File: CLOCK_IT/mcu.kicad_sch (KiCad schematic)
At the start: 25 parts, among them IC1 APS6404L-3SQR-SN, U1 ESP32-S3R8, U2 W25Q128JVSIQ

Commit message: :white_check_mark: Halffway here
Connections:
- net GND: now also U1.57 (GND)
- net USB_D+ renamed USB_DP
- net USB_D- renamed USB_DN
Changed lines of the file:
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@@
+	(wire
+		(pts
+			(xy 152.4 130.81) (xy 154.94 130.81)
+		)
+		(stroke
+			(width 0)
+			(type default)
+		)
+	)
 	(wire
 		(pts
@@
 		)
 	)
+	(label "USB_DP"
+		(at 162.56 102.87 180)
+		(effects
+			(font
+				(size 1.27 1.27)
+			)
+			(justify right bottom)
+		)
+	)
 	(label "Flash D"
 		(at 92.71 125.73 0)
@@
 		)
 	)
-	(label "USB_D+"
-		(at 162.56 102.87 180)
-		(effects
-			(font
-				(size 1.27 1.27)
-			)
-			(justify right bottom)
-		)
-	)
 	(label "XTAL_N"
 		(at 21.59 29.21 0)
@@
 			)
 			(justify left bottom)
+		)
+	)
+	(hierarchical_label "USB_DN"
+		(shape input)
+		(at 162.56 100.33 0)
+		(effects
+			(font
+				(size 1.27 1.27)
+			)
+			(justify left)
+		)
+	)
+	(hierarchical_label "USB_DP"
+		(shape input)
+		(at 162.56 102.87 0)
+		(effects
+			(font
+				(size 1.27 1.27)
+			)
+			(justify left)
 		)
 	)
@@
 					(unit 1)
 				)
+			)
+		)
+	)
+	(symbol
+		(lib_id "power:GND")
+		(at 154.94 130.81 0)
+		(unit 1)
+		(exclude_from_sim no)
+		(in_bom yes)
+		(on_board yes)
+		(dnp no)
+		(fields_autoplaced yes)
+		(property "Reference" "#PWR078"
+			(at 154.94 137.16 0)
+			(effects
+				(font
+					(size 1.27 1.27)
+				)
+				(hide yes)
+			)
+		)
+		(property "Value" "GND"
+			(at 154.94 135.89 0)
+			(effects
+				(font
+					(size 1.27 1.27)
+				)
+			)
+		)
+		(property "Footprint" ""
+			(at 154.94 130.81 0)
+			(effects
+				(font
+					(size 1.27 1.27)
+				)
+				(hide yes)
+			)
+		)
+		(property "Datasheet" ""
+			(at 154.94 130.81 0)
+			(effects
+				(font
+					(size 1.27 1.27)
+				)
+				(hide yes)
+			)
+		)
+		(property "Description" "Power symbol creates a global label with name \"GND\" , ground"
+			(at 154.94 130.81 0)
+			(effects
+				(font
+					(size 1.27 1.27)
+				)
+				(hide yes)
+			)
+		)
+		(pin "1"
+		)
+		(instances
+			(project "CLOCK_IT"
+				(path "/6c8f4e2a-0be1-4eb1-92e1-07339040f4c9/25a0942f-4692-4437-8e26-71d966c353a5"
+					(reference "#PWR078")
+					(unit 1)
+				)

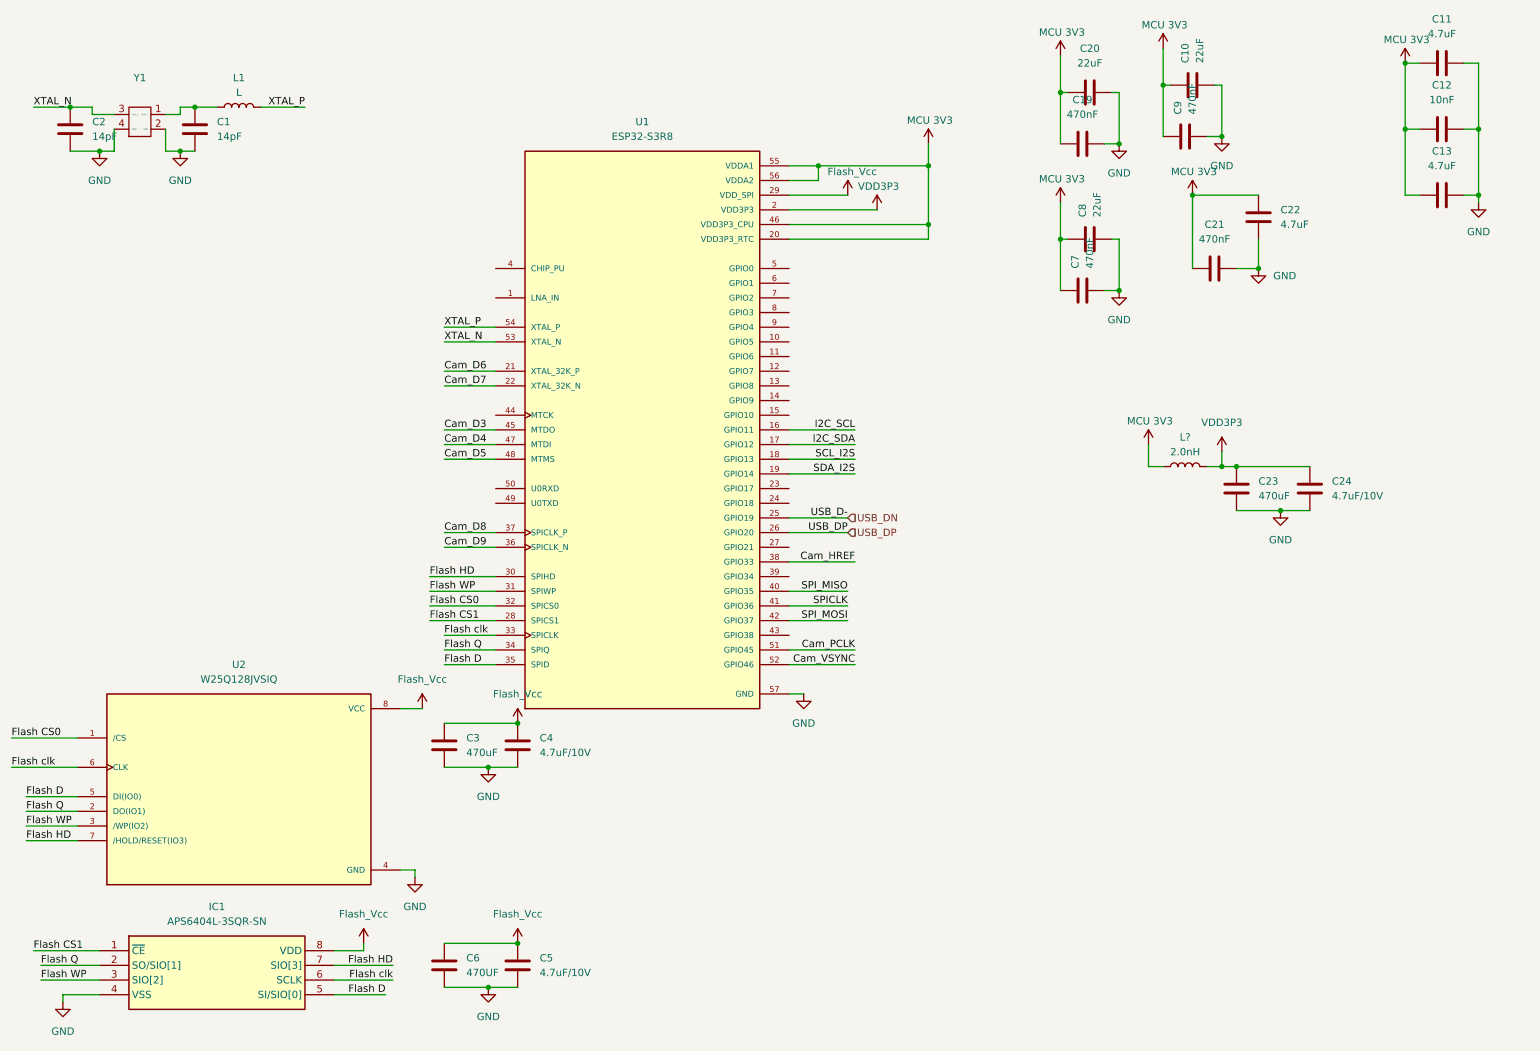
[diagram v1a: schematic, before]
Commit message: :white_check_mark: CHANGES in 12C pull up resisors
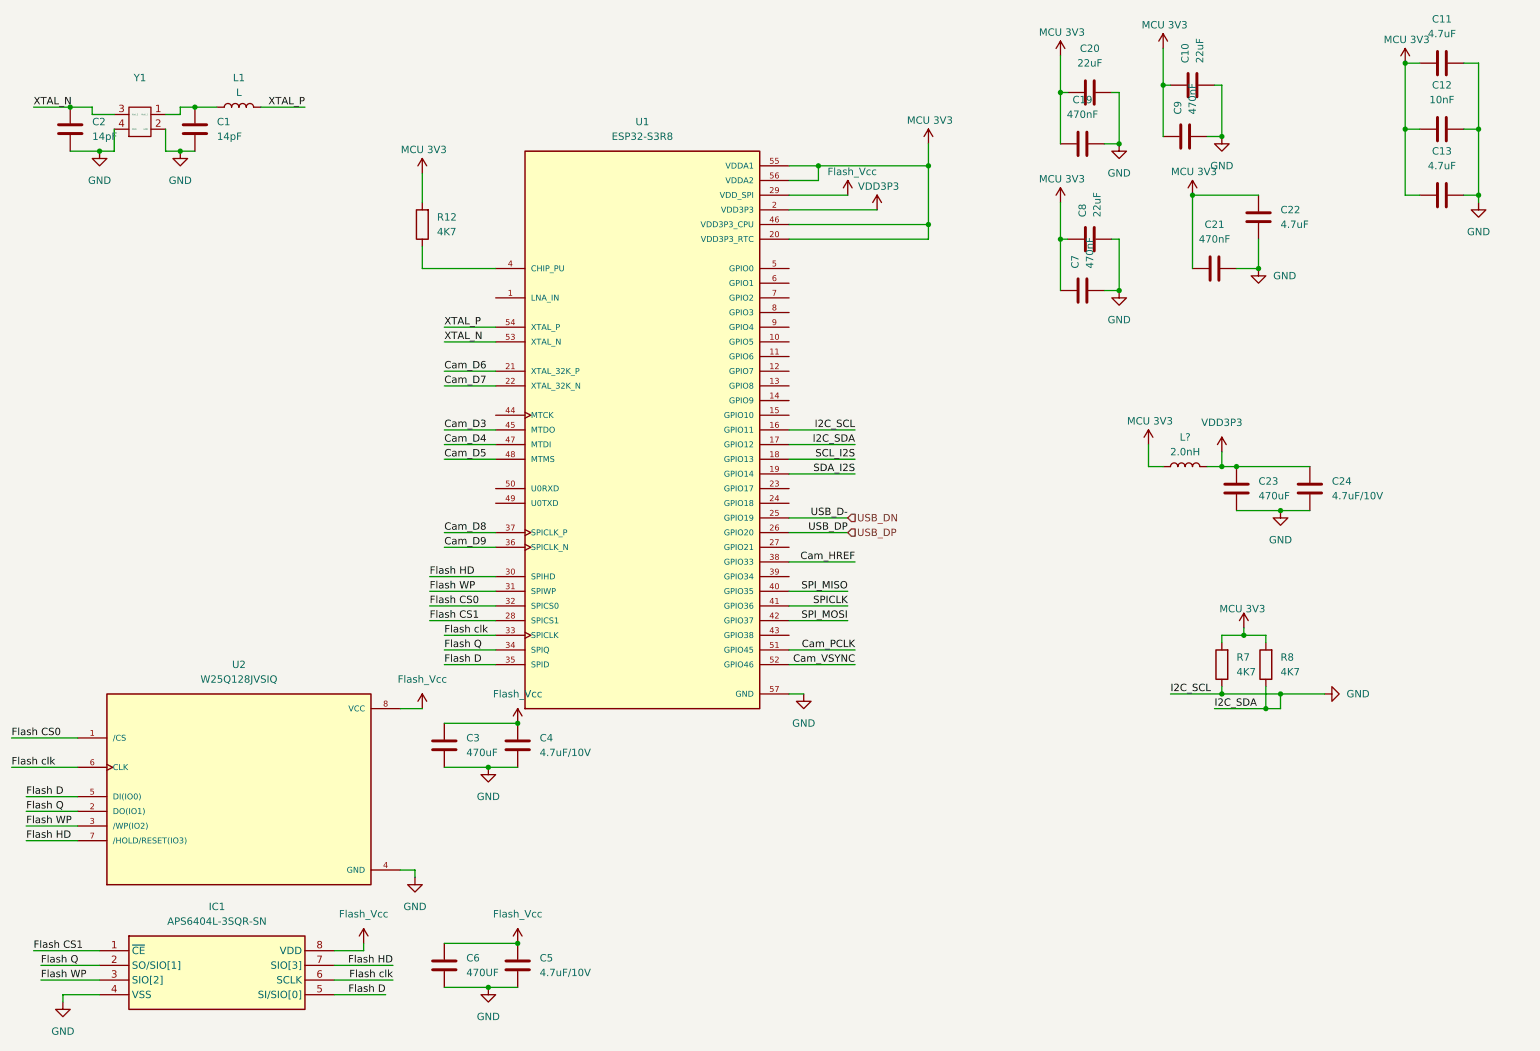
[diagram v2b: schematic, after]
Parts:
- added R12, R7, R8: 4K7, symbol Device:R
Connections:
- net I2C_SCL is gone; now on net GND: U1.16 (GPIO11)
- net I2C_SDA is gone; now on net GND: U1.17 (GPIO12)
- net GND: now also R7.1, R8.1
- net MCU 3V3: now also R12.2, R7.2, R8.2
- net at U1.4 (CHIP_PU): now also R12.1

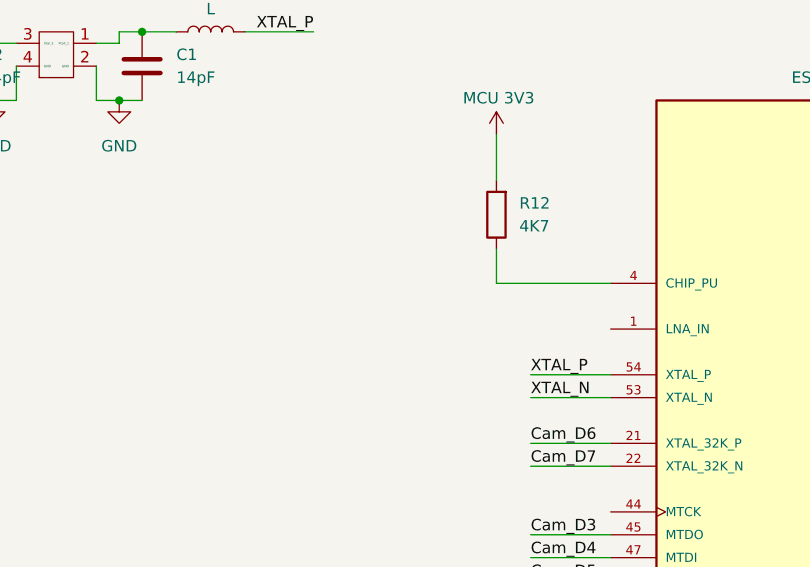
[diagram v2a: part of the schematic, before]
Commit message: :white_check_mark: added tacktile chip pu switch
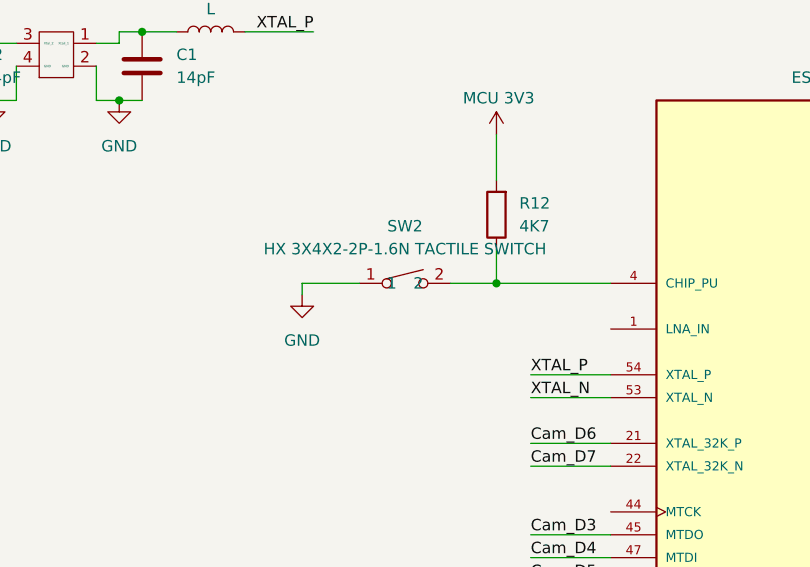
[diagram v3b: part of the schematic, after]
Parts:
- added SW2: HX 3X4X2-2P-1.6N TACTILE SWITCH, easyeda2kicad:KEY-SMD_L4.0-W3.0-LS4.9-1, symbol HX 3x4x2-2P-1.6N TACTILE SWITCH:HX3X4X2-2P-1.6NTACTILESWITCH
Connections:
- net GND: now also SW2.1
- net at R12.1, U1.4 (CHIP_PU): now also SW2.2
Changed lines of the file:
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@@
 	)
 	(junction
+		(at 88.9 57.15)
+		(diameter 0)
+		(color 0 0 0 0)
+	)
+	(junction
 		(at 229.87 91.44)
 		(diameter 0)
@@
 	(wire
 		(pts
+			(xy 67.31 57.15) (xy 73.66 57.15)
+		)
+		(stroke
+			(width 0)
+			(type default)
+		)
+	)
+	(wire
+		(pts
 			(xy 90.17 110.49) (xy 101.6 110.49)
 		)
@@
 	(wire
 		(pts
+			(xy 83.82 57.15) (xy 88.9 57.15)
+		)
+		(stroke
+			(width 0)
+			(type default)
+		)
+	)
+	(wire
+		(pts
 			(xy 209.55 52.07) (xy 208.28 52.07)
 		)
@@
 	(wire
 		(pts
+			(xy 67.31 58.42) (xy 67.31 57.15)
+		)
+		(stroke
+			(width 0)
+			(type default)
+		)
+	)
+	(wire
+		(pts
 			(xy 92.71 143.51) (xy 100.33 143.51)
 		)
@@
 	)
 	(symbol
+		(lib_id "HX 3x4x2-2P-1.6N TACTILE SWITCH:HX3X4X2-2P-1.6NTACTILESWITCH")
+		(at 78.74 55.88 0)
+		(unit 1)
+		(exclude_from_sim no)
+		(in_bom yes)
+		(on_board yes)
+		(dnp no)
+		(fields_autoplaced yes)
+		(property "Reference" "SW2"
+			(at 78.74 50.8 0)
+			(effects
+				(font
+					(size 1.27 1.27)
+				)
+			)
+		)
+		(property "Value" "HX 3X4X2-2P-1.6N TACTILE SWITCH"
+			(at 78.74 53.34 0)
+			(effects
+				(font
+					(size 1.27 1.27)
+				)
+			)
+		)
+		(property "Footprint" "easyeda2kicad:KEY-SMD_L4.0-W3.0-LS4.9-1"
+			(at 78.74 64.77 0)
+			(effects
+				(font
+					(size 1.27 1.27)
+				)
+				(hide yes)
+			)
+		)
+		(property "Datasheet" "https://www.lcsc.com/datasheet/C49234124.pdf"
+			(at 78.74 67.31 0)
+			(effects
+				(font
+					(size 1.27 1.27)
+				)
+				(hide yes)
+			)
+		)
+		(property "Description" ""
+			(at 78.74 55.88 0)
+			(effects
+				(font
+					(size 1.27 1.27)
+				)
+				(hide yes)
+			)
+		)
+		(property "Manufacturer" "hanxia(韩下)"
+			(at 78.74 69.85 0)
+			(effects
+				(font
+					(size 1.27 1.27)
+				)
+				(hide yes)
+			)
+		)
+		(property "MPN" "HX 3x4x2-2P-1.6N TACTILE SWITCH"
+			(at 78.74 72.39 0)
+			(effects
+				(font
+					(size 1.27 1.27)
+				)
+				(hide yes)
+			)
+		)
+		(property "LCSC Part" "C49234124"
+			(at 78.74 74.93 0)
+			(effects
+				(font
+					(size 1.27 1.27)
+				)
+				(hide yes)
+			)
+		)
+		(pin "1"
+		)
+		(pin "2"
+		)
+		(instances
+			(project ""
+				(path "/6c8f4e2a-0be1-4eb1-92e1-07339040f4c9/25a0942f-4692-4437-8e26-71d966c353a5"
+					(reference "SW2")
+					(unit 1)
+				)
+			)
+		)
+	)
+	(symbol
 		(lib_id "power:GND")
 		(at 46.99 36.83 0)
@@
 					(unit 1)
 				)
+			)
+		)
+	)
+	(symbol
+		(lib_id "power:GND")
+		(at 67.31 58.42 0)
+		(unit 1)
+		(exclude_from_sim no)
+		(in_bom yes)
+		(on_board yes)
+		(dnp no)
+		(fields_autoplaced yes)
+		(property "Reference" "#PWR082"
+			(at 67.31 64.77 0)
+			(effects
+				(font
+					(size 1.27 1.27)
+				)
+				(hide yes)
+			)
+		)
+		(property "Value" "GND"
+			(at 67.31 63.5 0)
+			(effects
+				(font
+					(size 1.27 1.27)
+				)
+			)
+		)
+		(property "Footprint" ""
+			(at 67.31 58.42 0)
+			(effects
+				(font
+					(size 1.27 1.27)
+				)
+				(hide yes)
+			)
+		)
+		(property "Datasheet" ""
+			(at 67.31 58.42 0)
+			(effects
+				(font
+					(size 1.27 1.27)
+				)
+				(hide yes)
+			)
+		)
+		(property "Description" "Power symbol creates a global label with name \"GND\" , ground"
+			(at 67.31 58.42 0)
+			(effects
+				(font
+					(size 1.27 1.27)
+				)
+				(hide yes)
+			)
+		)
+		(pin "1"
+		)
+		(instances
+			(project "CLOCK_IT"
+				(path "/6c8f4e2a-0be1-4eb1-92e1-07339040f4c9/25a0942f-4692-4437-8e26-71d966c353a5"
+					(reference "#PWR082")
+					(unit 1)
+				)

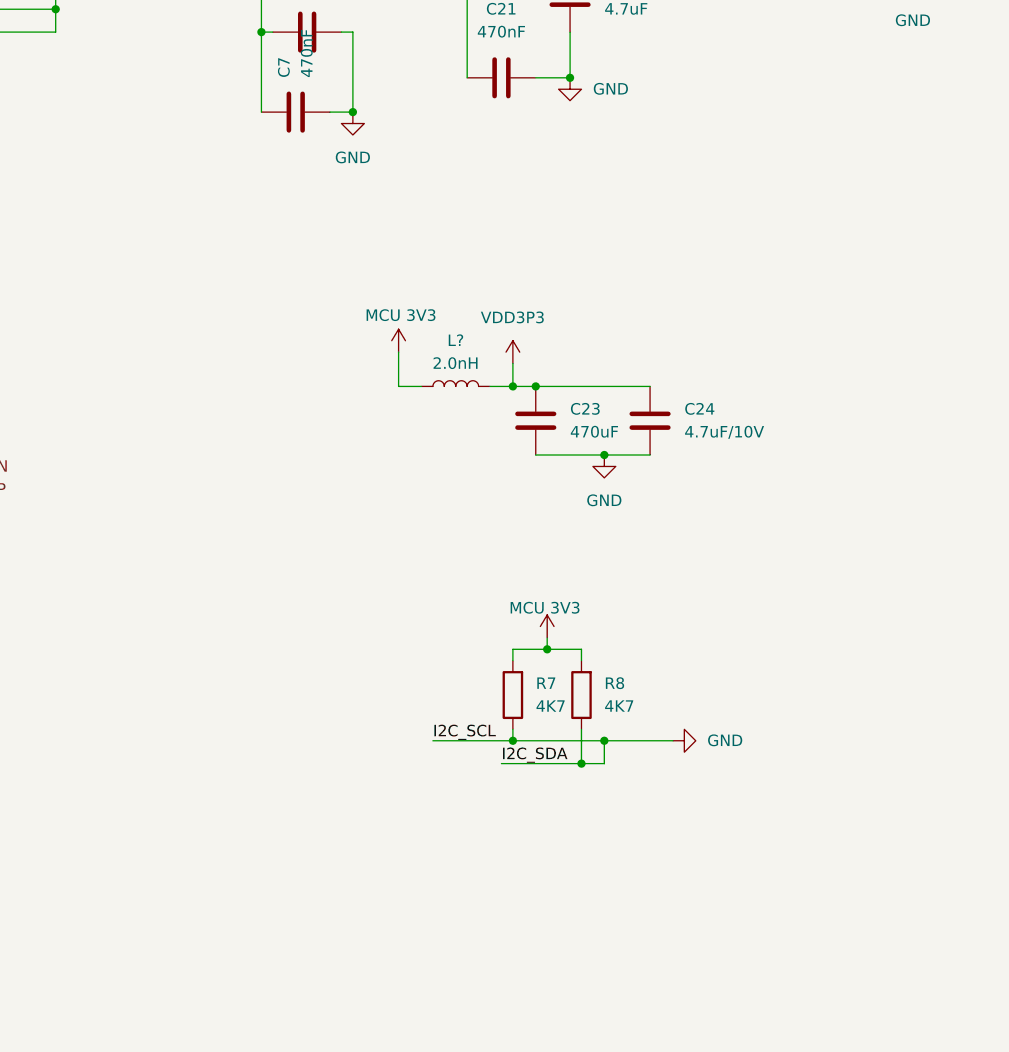
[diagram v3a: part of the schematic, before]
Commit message: :white_check_mark: Correcting I2C address conflicts with an i2c bus switch
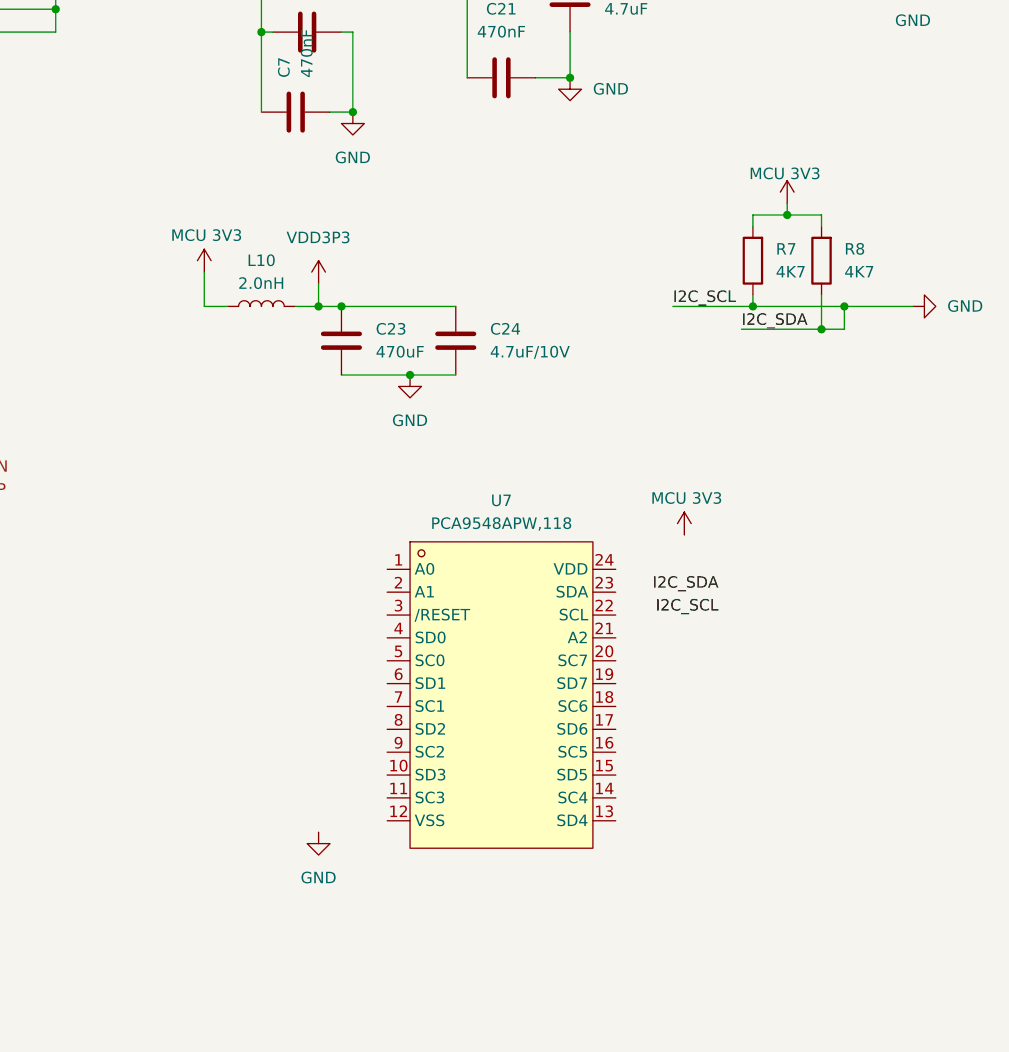
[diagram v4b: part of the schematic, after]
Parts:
- added U7: PCA9548APW,118, easyeda2kicad:TSSOP-24_L7.8-W4.4-P0.65-LS6.4-BL, symbol PCA9548APW,118:PCA9548APW,118
- gave numbers to parts that had none: 1
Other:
- moved on the sheet: C23, C24, L10, R7, R8

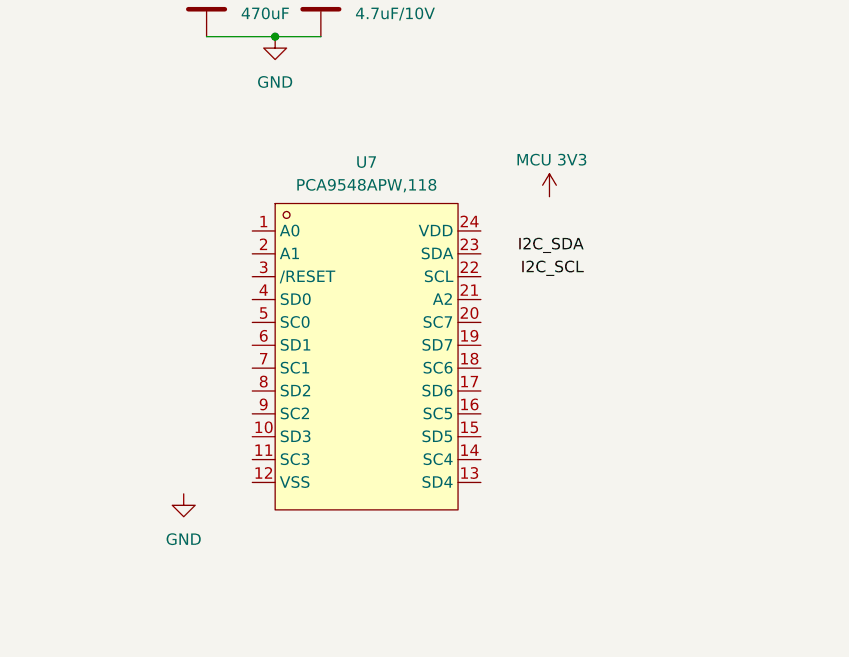
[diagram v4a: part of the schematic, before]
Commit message: :white_check_mark: Connected i2c bus switch
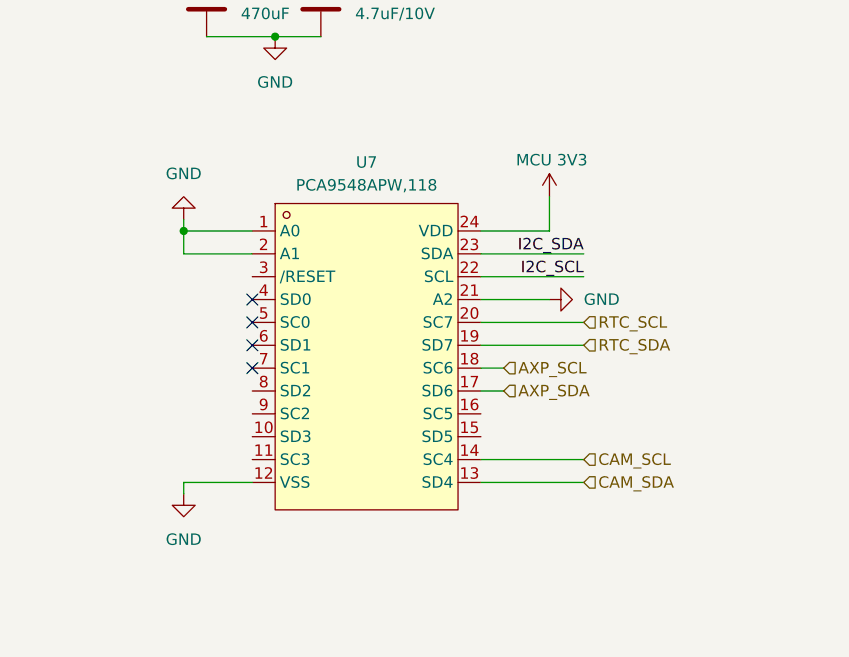
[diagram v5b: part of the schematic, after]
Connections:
- net GND: now also U7.1 (A0), U7.12 (VSS), U7.2 (A1), U7.21 (A2), U7.22 (SCL), U7.23 (SDA)
- net MCU 3V3: now also U7.24 (VDD)
- net CAM_SDA: now reaches U7.13 (SD4)
- net CAM_SCL: now reaches U7.14 (SC4)
- net AXP_SDA: now reaches U7.17 (SD6)
- net AXP_SCL: now reaches U7.18 (SC6)
- net RTC_SDA: now reaches U7.19 (SD7)
- net RTC_SCL: now reaches U7.20 (SC7)
- no-connect marks 0 -> 4
